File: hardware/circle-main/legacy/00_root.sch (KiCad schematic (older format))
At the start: 0 parts

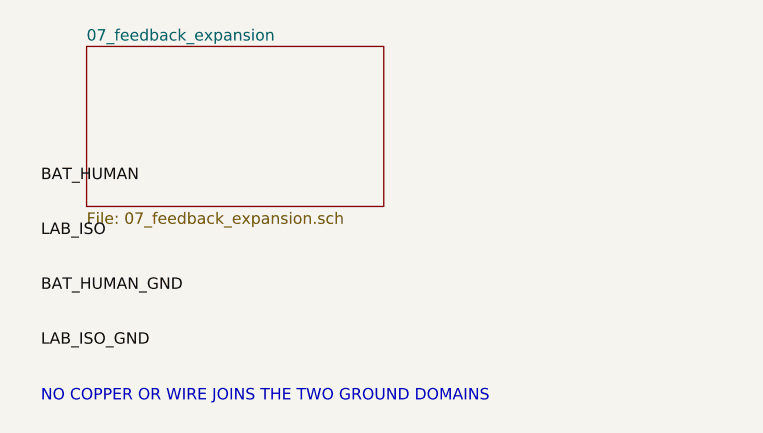
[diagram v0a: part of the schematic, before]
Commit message: Make every CIRCLE review claim reproducible
Validate and export the architecture-level schematics with KiCad 10.0.5, add zero-violation ERC gates, engineering documentation, and one-command evidence hashing.

Constraint: KiCad CLI does not import legacy .sch into native .kicad_sch

Rejected: Hand-written native S-expressions | would create unvalidated CAD

Confidence: medium

Scope-risk: broad

Reversibility: clean

Directive: Treat NET annotations as architecture interfaces, not fabrication-ready connectivity

Tested: py -3.11 tools/verify_release.py; 30 tests; KiCad 10.0.5 ERC/BOM/PDF/SVG/netlist exports

Not-tested: Native conversion, PCB layout, footprints, powered electrodes, human connection, EMC, or regulatory compliance
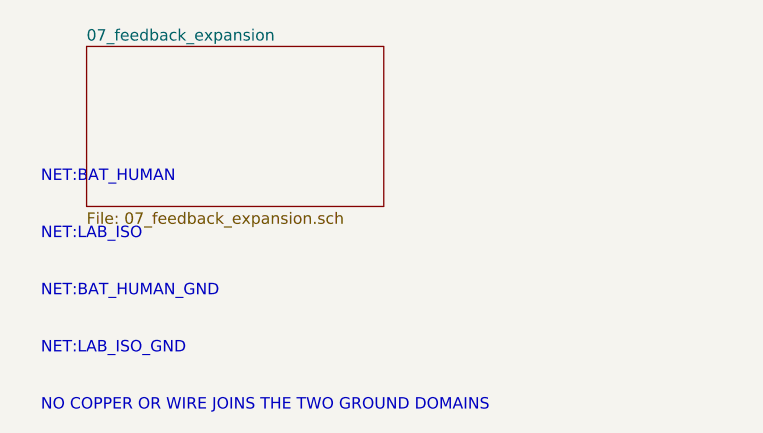
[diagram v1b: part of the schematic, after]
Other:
- note added: "NET:BAT_HUMAN"
- note added: "NET:BAT_HUMAN_GND"
- note added: "NET:LAB_ISO"
- note added: "NET:LAB_ISO_GND"
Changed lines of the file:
@@
 Sheet 1 1
 Title "Hierarchy and safety domains"
+Date "2026-08-14"
+Rev "A"
+Comp "Vers3Dynamics"
 Comment1 "ENGINEERING REVIEW ONLY - NOT FOR HUMAN CONNECTION"
+Comment2 "Generated artifact - edit manifest/generator"
+Comment3 ""
+Comment4 ""
 $EndDescr
 $Sheet
@@
 F1 "08_observability.sch" 50
 $EndSheet
-Text Label 700 5600 0    50   ~ 0
-BAT_HUMAN
-Text Label 700 5840 0    50   ~ 0
-LAB_ISO
-Text Label 700 6080 0    50   ~ 0
-BAT_HUMAN_GND
-Text Label 700 6320 0    50   ~ 0
-LAB_ISO_GND
 Text Notes 600 400 0    50   ~ 0
 ENGINEERING REVIEW ONLY - NOT FOR HUMAN CONNECTION
-Text Notes 700 6560 0    50   ~ 0
+Text Notes 700 5600 0    50   ~ 0
+NET:BAT_HUMAN
+Text Notes 700 5850 0    50   ~ 0
+NET:LAB_ISO
+Text Notes 700 6100 0    50   ~ 0
+NET:BAT_HUMAN_GND
+Text Notes 700 6350 0    50   ~ 0
+NET:LAB_ISO_GND
+Text Notes 700 6600 0    50   ~ 0
 NO COPPER OR WIRE JOINS THE TWO GROUND DOMAINS
 $EndSCHEMATC
